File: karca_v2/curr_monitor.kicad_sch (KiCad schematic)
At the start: 25 parts, among them U30 INA180A4, U31 INA180A4, U32 NUP4202

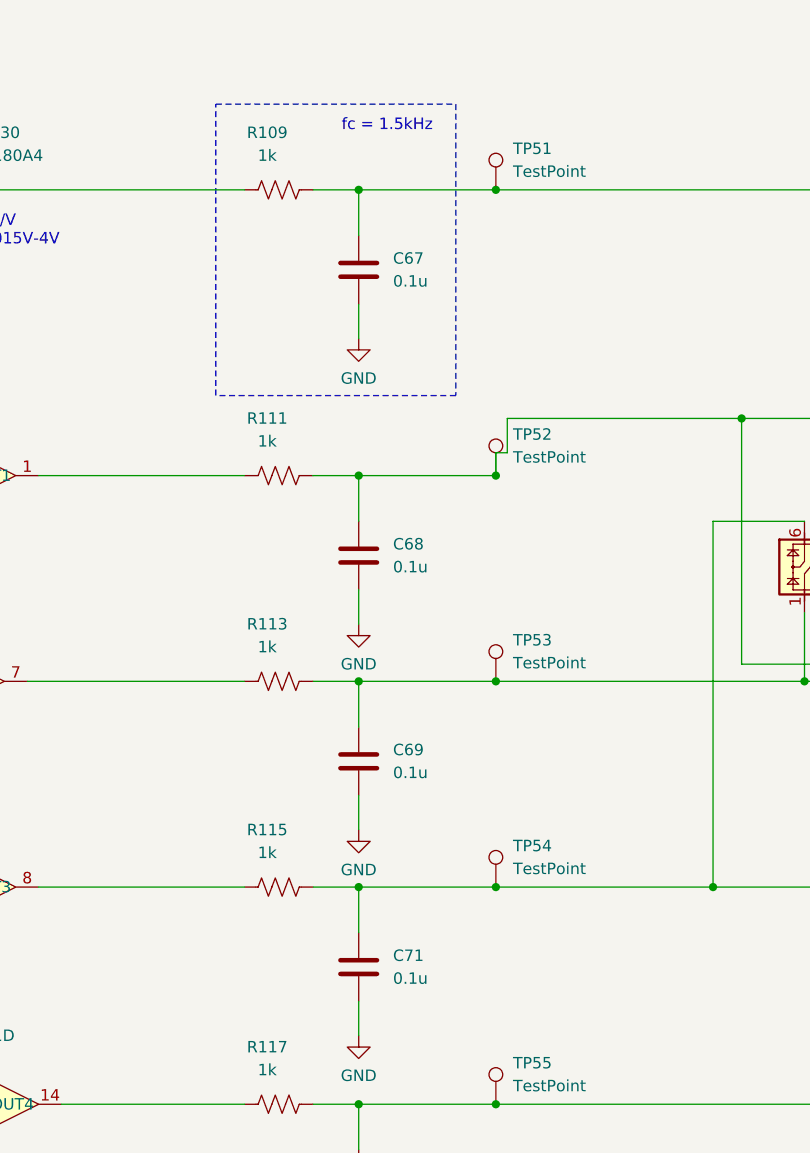
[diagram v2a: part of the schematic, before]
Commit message: finished schematic for v2.1
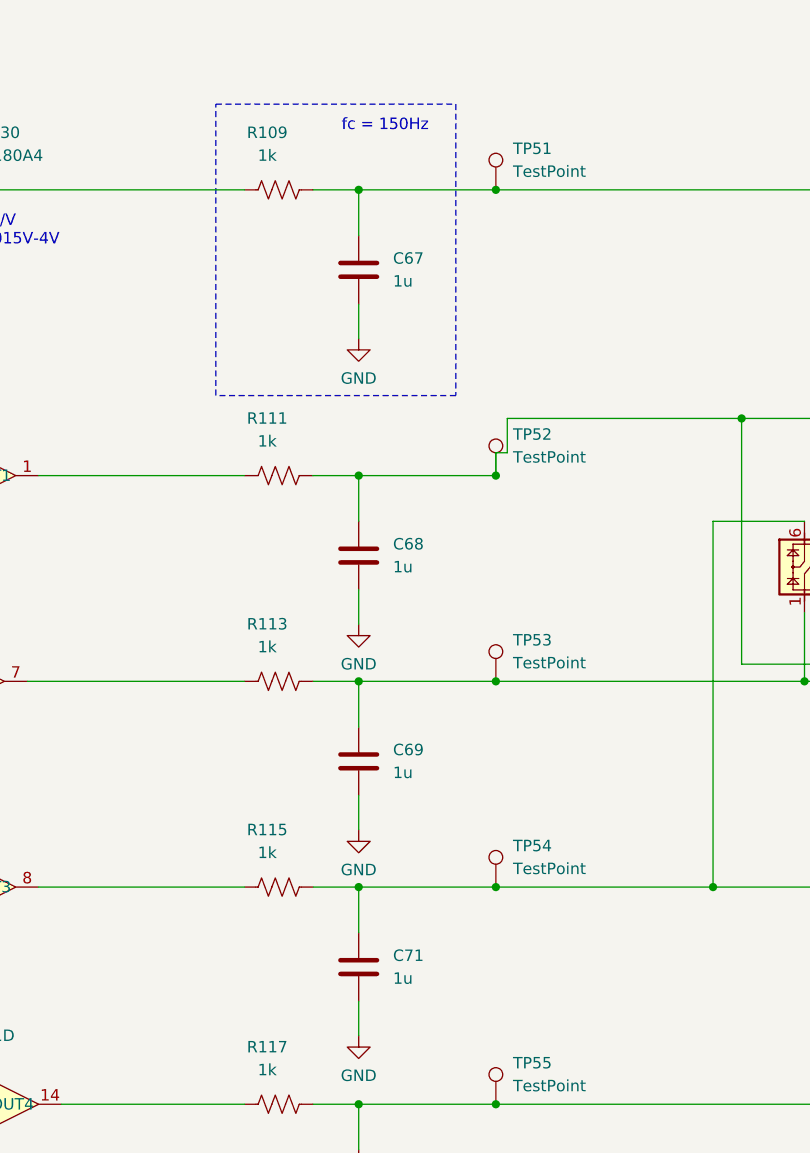
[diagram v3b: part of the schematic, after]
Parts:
- C67, C68, C69, C71: value 0.1u -> 1u
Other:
- note added: "fc = 150Hz"
- note removed: "fc = 1.5kHz"
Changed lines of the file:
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@@
 		)
 	)
-	(text "fc = 1.5kHz\n"
+	(text "fc = 150Hz\n"
 		(exclude_from_sim no)
 		(at 156.845 45.72 0)
@@
 			)
 		)
-		(property "Value" "0.1u"
+		(property "Value" "1u"
 			(at 162.56 93.98 0)
 			(effects
@@
 			)
 		)
-		(property "Value" "0.1u"
+		(property "Value" "1u"
 			(at 162.56 139.7 0)
 			(effects
@@
 			)
 		)
-		(property "Value" "0.1u"
+		(property "Value" "1u"
 			(at 162.56 62.23 0)
 			(effects
@@
 			)
 		)
-		(property "Value" "0.1u"
+		(property "Value" "1u"
 			(at 162.56 116.84 0)
 			(effects

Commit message: swapped adcs
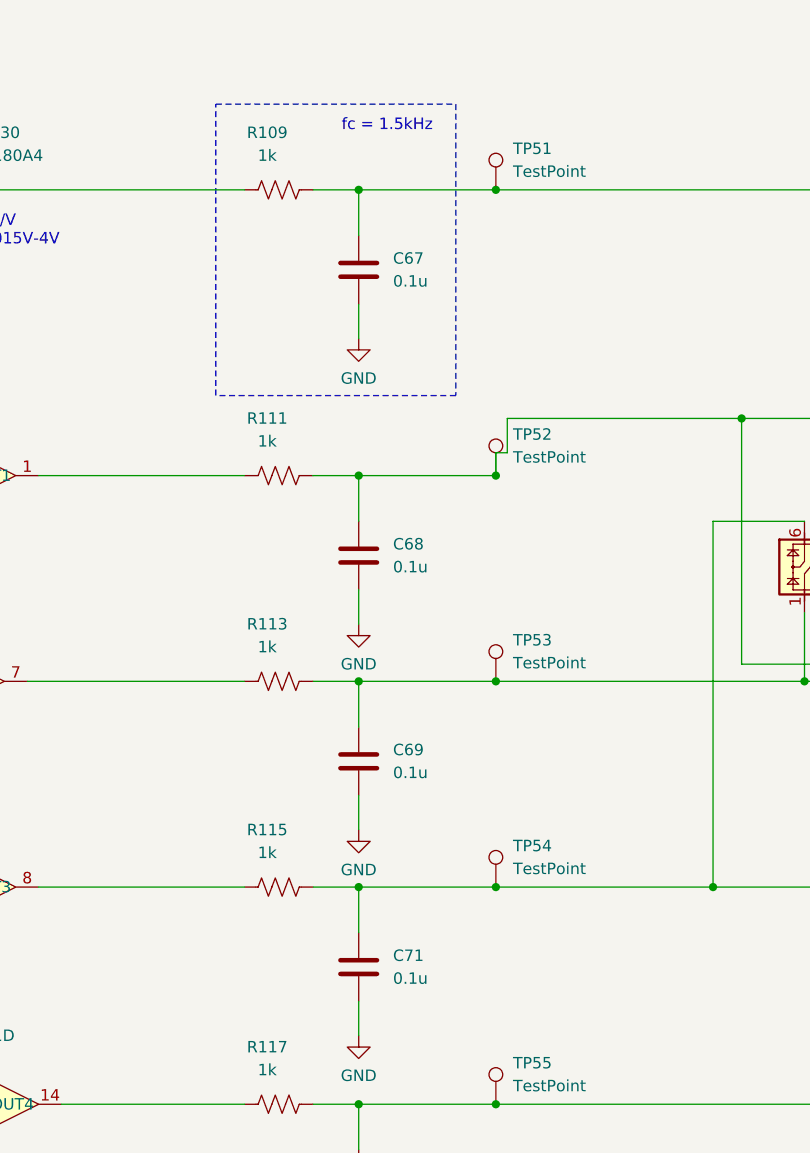
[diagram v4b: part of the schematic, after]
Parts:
- C67, C68, C69, C71: value 1u -> 0.1u
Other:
- note added: "fc = 1.5kHz"
- note removed: "fc = 150Hz"
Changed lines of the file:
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@@
 	(title_block
 		(title "kARCA 2.0 Engine Control System")
-		(date "2026-03-23")
-		(rev "1.2")
+		(date "2024-12-16")
+		(rev "1.1")
 		(company "Rice Eclipse")
 		(comment 1 "Designed by Deepak Narayan")
@@
 		)
 	)
-	(text "fc = 150Hz\n"
+	(text "fc = 1.5kHz\n"
 		(exclude_from_sim no)
 		(at 156.845 45.72 0)
@@
 			)
 		)
-		(property "Value" "1u"
+		(property "Value" "0.1u"
 			(at 162.56 93.98 0)
 			(effects
@@
 			)
 		)
-		(property "Value" "1u"
+		(property "Value" "0.1u"
 			(at 162.56 139.7 0)
 			(effects
@@
 			)
 		)
-		(property "Value" "1u"
+		(property "Value" "0.1u"
 			(at 162.56 62.23 0)
 			(effects
@@
 			)
 		)
-		(property "Value" "1u"
+		(property "Value" "0.1u"
 			(at 162.56 116.84 0)
 			(effects

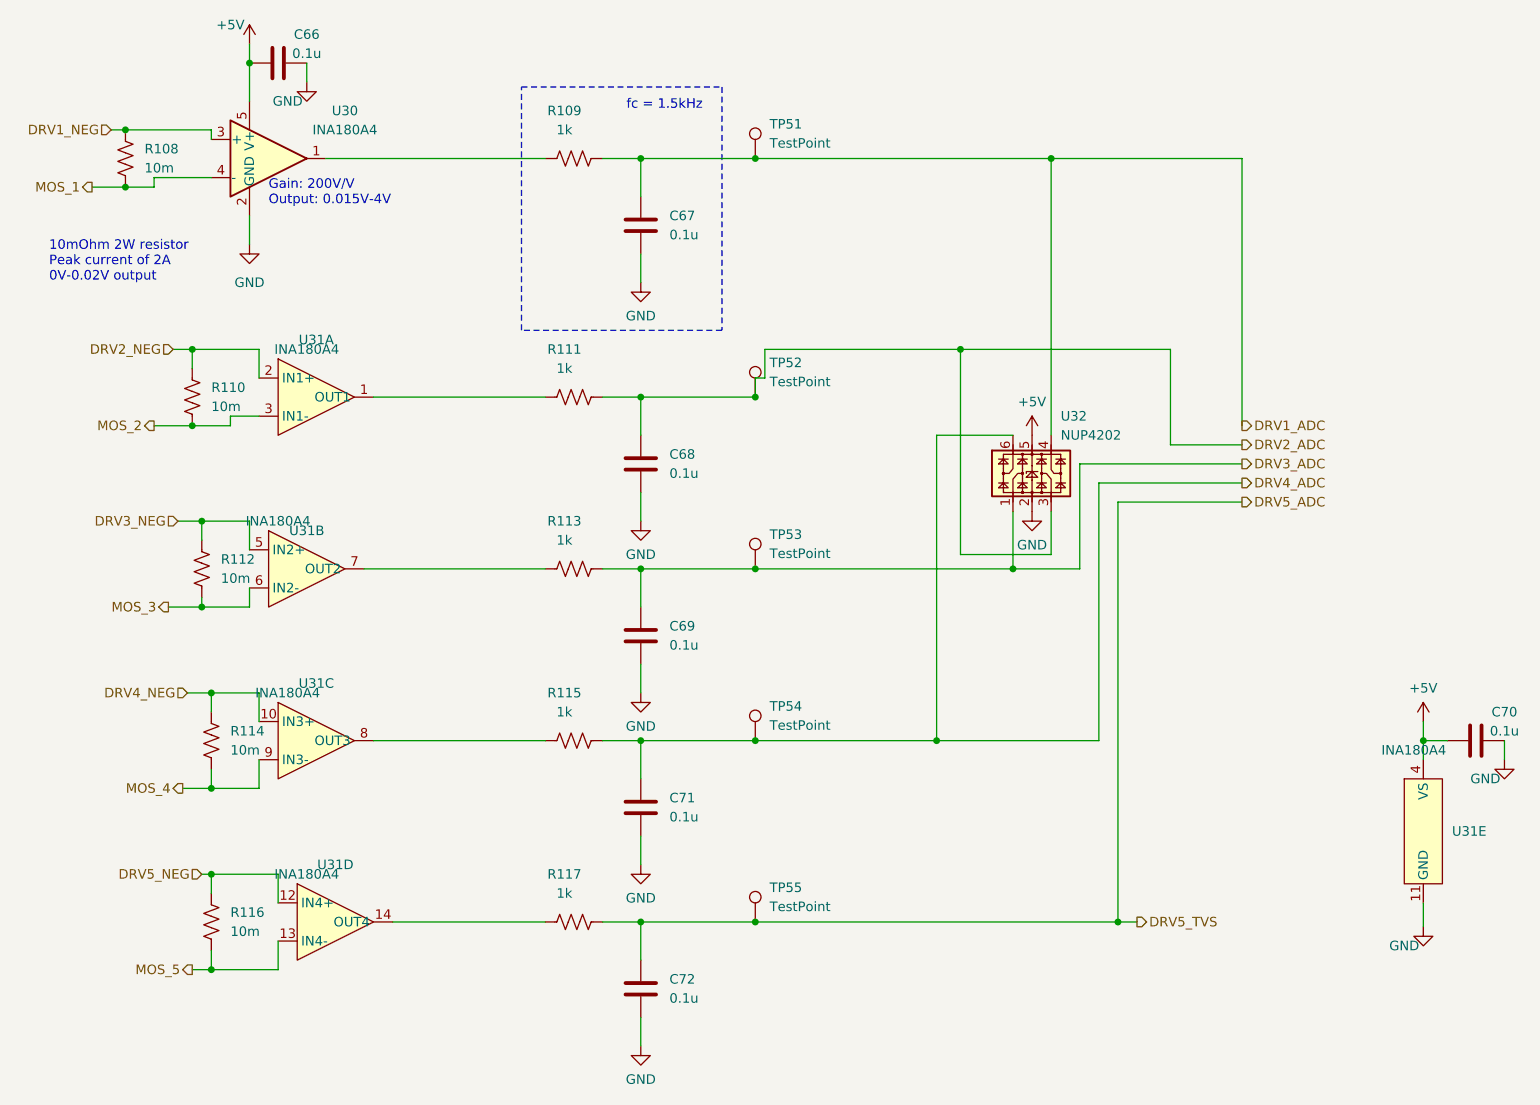
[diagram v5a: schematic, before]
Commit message: fixed all routing. Now need to clean up vias
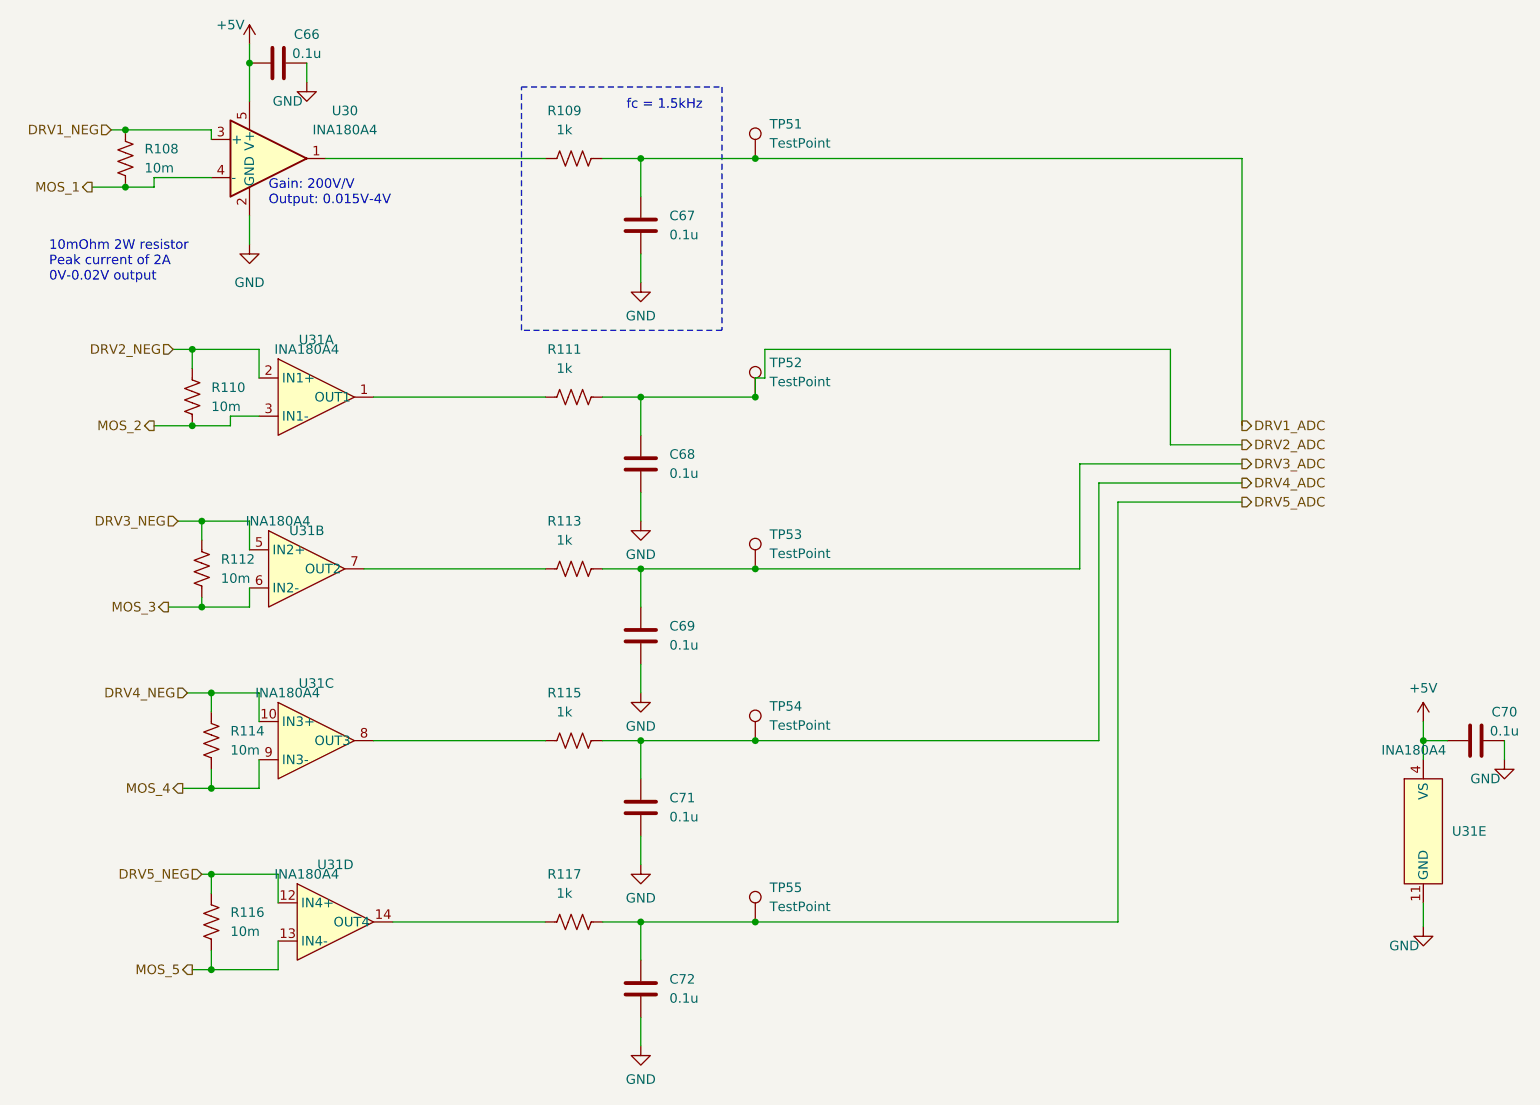
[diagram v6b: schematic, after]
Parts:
- removed U32: NUP4202, Package_TO_SOT_SMD:SOT-363_SC-70-6, symbol Power_Protection:NUP4202

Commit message: final production version
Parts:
- U30: MPN (none) -> C133969
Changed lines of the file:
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@@
+			)
+		)
+		(property "MPN" "C133969"
+			(at 109.22 52.07 0)
+			(effects
+				(font
+					(size 1.27 1.27)
+				)
+				(hide yes)
 			)
 		)
